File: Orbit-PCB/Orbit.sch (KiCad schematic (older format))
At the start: 280 parts, among them J1 PJ-3200B-4A, J10 Breakaway_Tabs, J11 PJ-3200B-4A, J12 AVR-ISP-6, J13 Breakaway_Tabs, J14 Breakaway_Tabs, J17 Breakaway_Tabs, J18 Breakaway_Tabs, J19 Breakaway_Tabs, J2 AVR-ISP-6, J20 Breakaway_Tabs, J3 Breakaway_Tabs, J5 Breakaway_Tabs, J6 Breakaway_Tabs, J7 Breakaway_Tabs, J9 Breakaway_Tabs, Q1 2N7002, Q2 2N7002, SW1 SW_Push, SW2 SW_Push, U1 ATmega32U4-MU, U2 PRTR5V0U2X, U3 ATmega32U4-MU, U4 PRTR5V0U2X, Y1 16MHz, Y2 16MHz

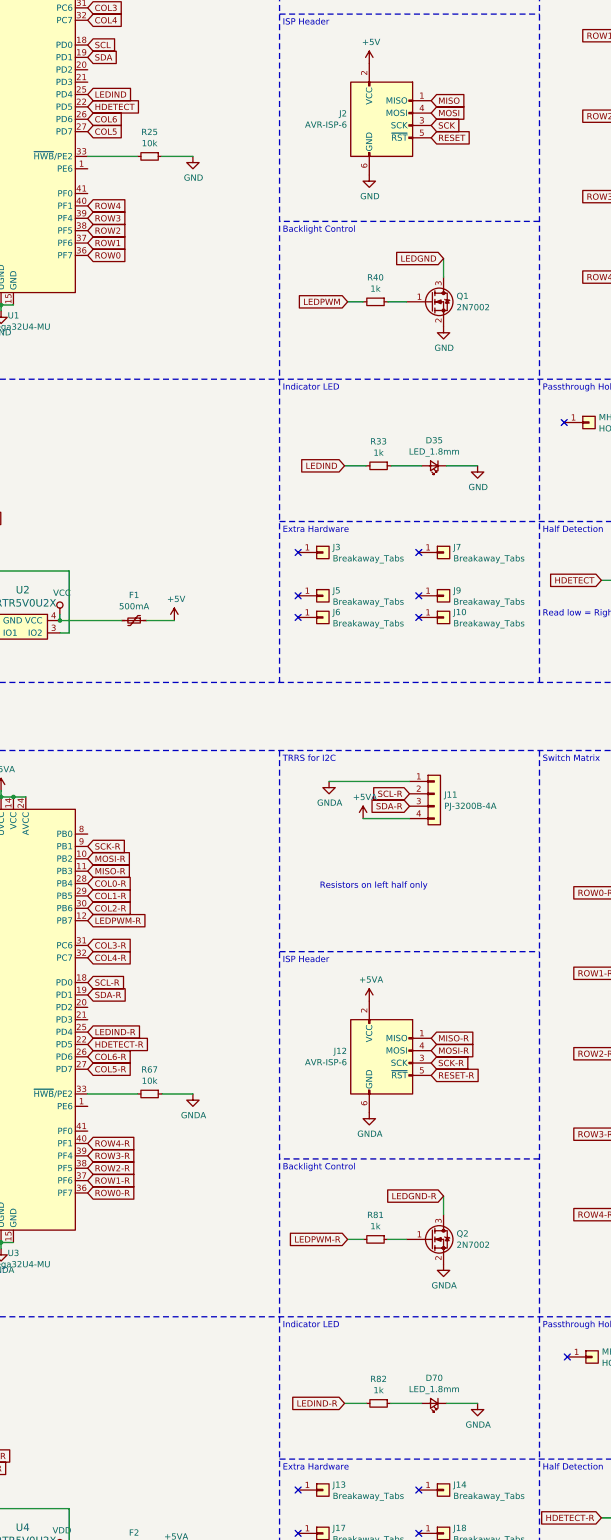
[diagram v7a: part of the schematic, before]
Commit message: Route status LEDs
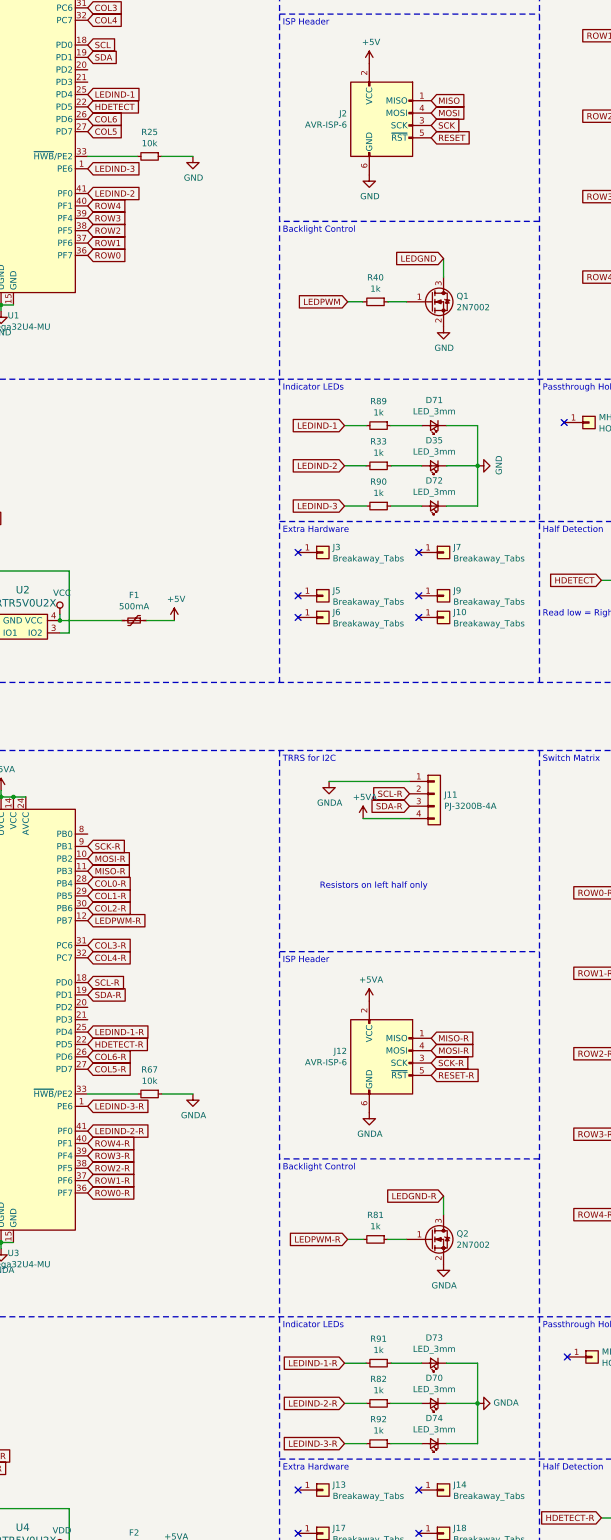
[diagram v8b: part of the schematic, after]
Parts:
- added D71, D72, D73, D74: LED_3mm, locallib:LED_D3.0mm, symbol Device:LED_Small
- added R89, R90, R91, R92: 1k, Resistors_SMD:R_0805, symbol Device:R_Small
- D35, D70: value LED_1.8mm -> LED_3mm; footprint LEDs:LED_D3.0mm -> locallib:LED_D3.0mm
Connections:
- net labels added: LEDIND-1, LEDIND-1-R, LEDIND-2, LEDIND-2-R, LEDIND-3, LEDIND-3-R
- net labels removed: LEDIND, LEDIND-R
- wire segments 635 -> 651
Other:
- note added: "Indicator LEDs\n"
- note removed: "Indicator LED"
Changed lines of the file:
@@
 P 6900 5950
 F 0 "D35" H 6900 5745 50  0000 C CNN
-F 1 "LED_1.8mm" H 6900 5836 50  0000 C CNN
-F 2 "LEDs:LED_D3.0mm" V 6900 5950 50  0001 C CNN
+F 1 "LED_3mm" H 6900 5836 50  0000 C CNN
+F 2 "locallib:LED_D3.0mm" V 6900 5950 50  0001 C CNN
 F 3 "~" V 6900 5950 50  0001 C CNN
 	1    6900 5950
@@
 F 3 "" H 7250 5950 50  0001 C CNN
 	1    7250 5950
-	1    0    0    -1
+	0    -1   -1   0
 $EndComp
 Wire Wire Line
 	7250 5950 7000 5950
 Text GLabel 6175 5950 0    50   Input ~ 0
-LEDIND
+LEDIND-2
 Wire Wire Line
 	6175 5950 6350 5950
 Text Notes 5675 5350 0    50   ~ 0
-Indicator LED
+Indicator LEDs\n
 Text GLabel 4100 1750 2    50   Input ~ 0
 COL0
@@
 ROW4
 Text GLabel 4100 2950 2    50   Input ~ 0
-LEDIND
+LEDIND-1
 Wire Notes Line
 	7750 675  7750 7700
@@
 P 6900 13525
 F 0 "D70" H 6900 13320 50  0000 C CNN
-F 1 "LED_1.8mm" H 6900 13411 50  0000 C CNN
-F 2 "LEDs:LED_D3.0mm" V 6900 13525 50  0001 C CNN
+F 1 "LED_3mm" H 6900 13411 50  0000 C CNN
+F 2 "locallib:LED_D3.0mm" V 6900 13525 50  0001 C CNN
 F 3 "~" V 6900 13525 50  0001 C CNN
 	1    6900 13525
@@
 	7250 13525 7000 13525
 Text GLabel 6175 13525 0    50   Input ~ 0
-LEDIND-R
+LEDIND-2-R
 Wire Wire Line
 	6175 13525 6350 13525
 Text Notes 5675 12925 0    50   ~ 0
-Indicator LED
+Indicator LEDs\n
 Text GLabel 4100 9325 2    50   Input ~ 0
 COL0-R
@@
 ROW4-R
 Text GLabel 4100 10525 2    50   Input ~ 0
-LEDIND-R
+LEDIND-1-R
 Wire Notes Line
 	7750 8250 7750 15275
@@
 P 7250 13525
 F 0 "#PWR0130" H 7250 13275 50  0001 C CNN
-F 1 "GNDA" H 7255 13352 50  0000 C CNN
+F 1 "GNDA" V 7255 13397 50  0000 R CNN
 F 2 "" H 7250 13525 50  0001 C CNN
 F 3 "" H 7250 13525 50  0001 C CNN
 	1    7250 13525
-	1    0    0    -1
+	0    -1   -1   0
 $EndComp
 $Comp
@@
 	13075 4025 12825 4025
 Connection ~ 12825 4025
+$Comp
+L Device:R_Small R89
+U 1 1 5DA6BD82
+P 6450 5625
+F 0 "R89" V 6254 5625 50  0000 C CNN
+F 1 "1k" V 6345 5625 50  0000 C CNN
+F 2 "Resistors_SMD:R_0805" H 6450 5625 50  0001 C CNN
+F 3 "~" H 6450 5625 50  0001 C CNN
+	1    6450 5625
+	0    1    1    0
+$EndComp
+$Comp
+L Device:LED_Small D71
+U 1 1 5DA6BD89
+P 6900 5625
+F 0 "D71" H 6900 5420 50  0000 C CNN
+F 1 "LED_3mm" H 6900 5511 50  0000 C CNN
+F 2 "locallib:LED_D3.0mm" V 6900 5625 50  0001 C CNN
+F 3 "~" V 6900 5625 50  0001 C CNN
+	1    6900 5625
+	-1   0    0    1
+$EndComp
+Wire Wire Line
+	6800 5625 6550 5625
+Text GLabel 6175 5625 0    50   Input ~ 0
+LEDIND-1
+Wire Wire Line
+	6175 5625 6350 5625
+Wire Wire Line
+	7000 5625 7250 5625
+Wire Wire Line
+	7250 5625 7250 5950
+Connection ~ 7250 5950
+$Comp
+L Device:R_Small R90
+U 1 1 5DB56624
+P 6450 6275
+F 0 "R90" V 6254 6275 50  0000 C CNN
+F 1 "1k" V 6345 6275 50  0000 C CNN
+F 2 "Resistors_SMD:R_0805" H 6450 6275 50  0001 C CNN
+F 3 "~" H 6450 6275 50  0001 C CNN
+	1    6450 6275
+	0    1    1    0
+$EndComp
+$Comp
+L Device:LED_Small D72
+U 1 1 5DB5662B
+P 6900 6275
+F 0 "D72" H 6900 6070 50  0000 C CNN
+F 1 "LED_3mm" H 6900 6161 50  0000 C CNN
+F 2 "locallib:LED_D3.0mm" V 6900 6275 50  0001 C CNN
+F 3 "~" V 6900 6275 50  0001 C CNN
+	1    6900 6275
+	-1   0    0    1
+$EndComp
+Wire Wire Line
+	6800 6275 6550 6275
+Text GLabel 6175 6275 0    50   Input ~ 0
+LEDIND-3
+Wire Wire Line
+	6175 6275 6350 6275
+Wire Wire Line
+	7000 6275 7250 6275
+Wire Wire Line
+	7250 6275 7250 5950
+$Comp
+L Device:R_Small R91
+U 1 1 5DC48BA4
+P 6450 13200
+F 0 "R91" V 6254 13200 50  0000 C CNN
+F 1 "1k" V 6345 13200 50  0000 C CNN
+F 2 "Resistors_SMD:R_0805" H 6450 13200 50  0001 C CNN
+F 3 "~" H 6450 13200 50  0001 C CNN
+	1    6450 13200
+	0    1    1    0
+$EndComp
+$Comp
+L Device:LED_Small D73
+U 1 1 5DC48BAB
+P 6900 13200
+F 0 "D73" H 6900 12995 50  0000 C CNN
+F 1 "LED_3mm" H 6900 13086 50  0000 C CNN
+F 2 "locallib:LED_D3.0mm" V 6900 13200 50  0001 C CNN
+F 3 "~" V 6900 13200 50  0001 C CNN
+	1    6900 13200
+	-1   0    0    1
+$EndComp
+Wire Wire Line
+	6800 13200 6550 13200
+Text GLabel 6175 13200 0    50   Input ~ 0
+LEDIND-1-R
+Wire Wire Line
+	6175 13200 6350 13200
+Wire Wire Line
+	7000 13200 7250 13200
+Wire Wire Line
+	7250 13200 7250 13525
+Connection ~ 7250 13525
+$Comp
+L Device:R_Small R92
+U 1 1 5DEA831B
+P 6450 13850
+F 0 "R92" V 6254 13850 50  0000 C CNN
+F 1 "1k" V 6345 13850 50  0000 C CNN
+F 2 "Resistors_SMD:R_0805" H 6450 13850 50  0001 C CNN
+F 3 "~" H 6450 13850 50  0001 C CNN
+	1    6450 13850
+	0    1    1    0
+$EndComp
+$Comp
+L Device:LED_Small D74
+U 1 1 5DEA8322
+P 6900 13850
+F 0 "D74" H 6900 13645 50  0000 C CNN
+F 1 "LED_3mm" H 6900 13736 50  0000 C CNN
+F 2 "locallib:LED_D3.0mm" V 6900 13850 50  0001 C CNN
+F 3 "~" V 6900 13850 50  0001 C CNN
+	1    6900 13850
+	-1   0    0    1
+$EndComp
+Wire Wire Line
+	6800 13850 6550 13850
+Text GLabel 6175 13850 0    50   Input ~ 0
+LEDIND-3-R
+Wire Wire Line
+	6175 13850 6350 13850
+Wire Wire Line
+	7000 13850 7250 13850
+Wire Wire Line
+	7250 13850 7250 13525
+Text GLabel 4100 3750 2    50   Input ~ 0
+LEDIND-2
+Text GLabel 4100 3550 2    50   Input ~ 0
+LEDIND-3
+Text GLabel 4100 11325 2    50   Input ~ 0
+LEDIND-2-R
+Text GLabel 4100 11125 2    50   Input ~ 0
+LEDIND-3-R
 $EndSCHEMATC
